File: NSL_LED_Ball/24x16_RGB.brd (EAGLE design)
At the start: 46.4 x 123.7 mm, 90 parts, among them IC1 TLC5947XLP, IC2 TLC5947XLP, IC3 TLC5947XLP, IC4 MEGA8-AI, IC5 MCP73123, IC6 BLUETOOTH-RN41", IC7 MMA7455L, IC8 OPA344, X1 16Mhz

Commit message: 
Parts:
- removed F1: 1206L150/12SLYR, SparkFun:PTC-1206
- LED1, LED10, LED11, LED12, LED13, LED14, LED15, LED16, LED17, LED18, LED19, LED2, LED20, LED21, LED22, LED23, LED24, LED3, LED4, LED5, LED6, LED7, LED8, LED9: device 16x16_RGB:LED5MM_RGB_EDGE -> 24x16_RGB:LED5MM_RGB_EDGE
- moved TP10 4.27 mm to (-24.2, -2.49)
- moved TP3 4.12 mm to (-20.2, -2.49)
- moved TP8 2.41 mm to (-22.2, -2.49)
- moved TP7 2.32 mm to (-20.2, -2.49)
- moved TP12 1.30 mm to (-22.2, -2.49)
- moved TP4 1.30 mm to (-24.2, -2.49)
- moved TP1 0.76 mm to (-22.1, 2.72)
- moved TP11 0.76 mm to (-20.1, 2.72)
- moved TP2 0.76 mm to (-24.1, 2.72)
- moved TP5 0.76 mm to (-22.1, 2.72)
- moved TP6 0.76 mm to (-24.1, 2.72)
- moved TP9 0.76 mm to (-20.1, 2.72)
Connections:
- removed net VBAT: BATTERY.2, C7.A, F1.1, IC5.3, IC5.4
- net VCC: now also BATTERY.2, C7.A, IC5.3, IC5.4; no longer F1.2
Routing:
- net VCC: track 416.3 -> 434.0 mm
- net VBAT: track 16.2 -> 0.00 mm
- net SCLK: track 154.8 -> 150.3 mm
- net CHARGE: track 10.1 -> 12.5 mm
- net SIN: track 92.7 -> 90.5 mm
- net MIC: track 56.0 -> 53.9 mm
- net SOUT: track 61.4 -> 62.8 mm
- net COL58: track 7.22 -> 8.36 mm
- net COL25: track 23.1 -> 24.2 mm
- net COL31: track 11.5 -> 12.4 mm
- net COL37: track 5.72 -> 4.83 mm
- net COL19: track 14.5 -> 13.7 mm
- net COL72: track 22.0 -> 22.8 mm
- net COL13: track 5.57 -> 4.72 mm
- net COL28: track 17.6 -> 18.5 mm
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
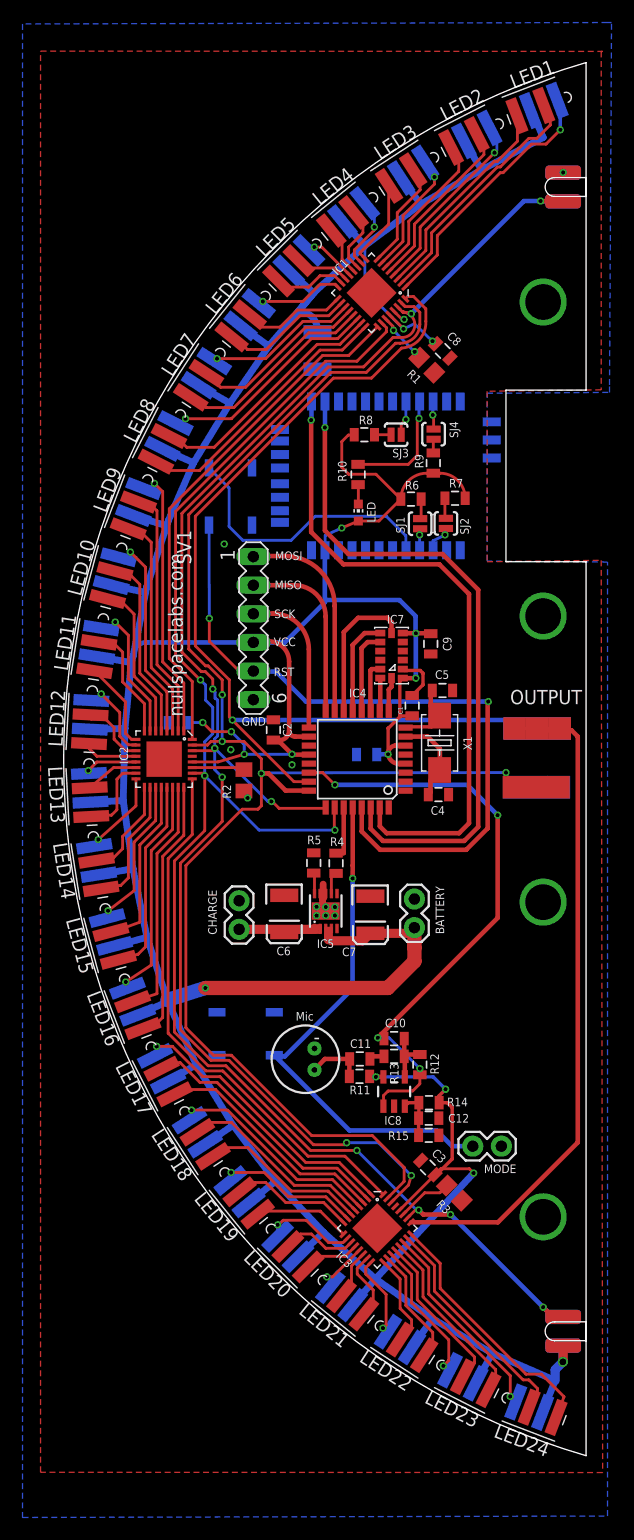
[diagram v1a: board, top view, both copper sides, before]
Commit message: 
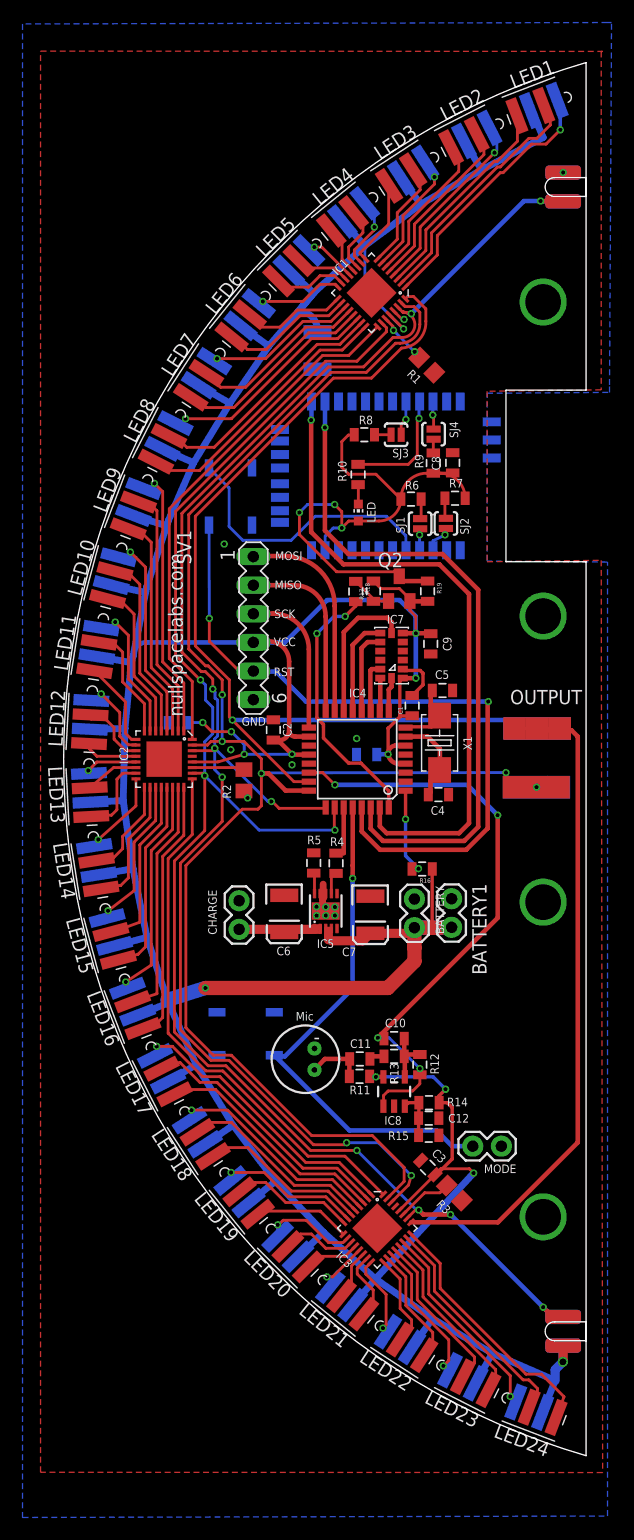
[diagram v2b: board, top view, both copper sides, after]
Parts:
- added BATTERY1: (no value), SparkFun:1X02
- added Q2: BSH201, transistor-small-signal:SOT23
- added R16: 220K, slice_noshift:0805
- added R17, R18: 10k, SparkFun:0805
- added R19: 0ohm DNP, SparkFun:0805
- moved C8 9.97 mm to (-29.6, 26.3), turned to 90 degrees
- moved TP12 1.98 mm to (-20.2, -2.49)
- moved TP3 1.98 mm to (-22.2, -2.49)
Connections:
- new net BT_PWR: IC4.32, R18.2
- new net N$18: Q2.1, R17.1, R18.1
- new net VDD: C8.1, IC6.11, LED.A, Q2.3, R19.1, R6.2, R7.2, R8.2, R9.2
- net BATTSENSE: now also R16.2
- net GND: now also BATTERY1.1
- net VCC: now also BATTERY1.2, Q2.2, R16.1, R17.2, R19.2; no longer C8.1, IC6.11, LED.A, R6.2, R7.2, R8.2, R9.2
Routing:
- net VDD: track 0.00 -> 49.4 mm, vias 0 -> 3
- net BT_PWR: track 0.00 -> 23.6 mm, vias 0 -> 2
- net VCC: track 434.0 -> 419.8 mm, vias 15 -> 13
- net BATTSENSE: track 0.00 -> 7.98 mm, vias 0 -> 2
- net SCLK: track 150.3 -> 154.3 mm, vias 4 -> 5
- net N$18: track 0.00 -> 3.78 mm
- net GND: vias 12 -> 13
